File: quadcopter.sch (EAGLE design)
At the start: 65 parts, among them J1 AVR_SPI_PRG_6NS, Q1 N-CHANNEL_MOSFET, Q2 N-CHANNEL_MOSFET, Q3 N-CHANNEL_MOSFET, Q4 N-CHANNEL_MOSFET, U1 ATMEGA128RFA1

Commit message: Did board work, renamed flyback and filtered in schematic
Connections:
- removed net FILTERED: Q1.GND, Q2.GND, Q3.GND, Q4.GND, R10.2, R11.2, R2.2, R3.2, R4.2, R7.2, R8.2, R9.2
- removed net FLYBACK: D1.A, D6.A, D7.A, D8.A, Q1.D, Q2.D, Q3.D, Q4.D, U$1.V-, U$2.V-, U$3.V-, U$4.V-
- new net FILTERED1: Q1.GND, R2.2, R3.2
- new net FILTERED2: Q2.GND, R4.2, R7.2
- new net FILTERED3: Q3.GND, R8.2, R9.2
- new net FILTERED4: Q4.GND, R10.2, R11.2
- new net FLYBACK1: D1.A, Q1.D, U$1.V-
- new net FLYBACK2: D6.A, Q2.D, U$2.V-
- new net FLYBACK3: D7.A, Q3.D, U$3.V-
- new net FLYBACK4: D8.A, Q4.D, U$4.V-

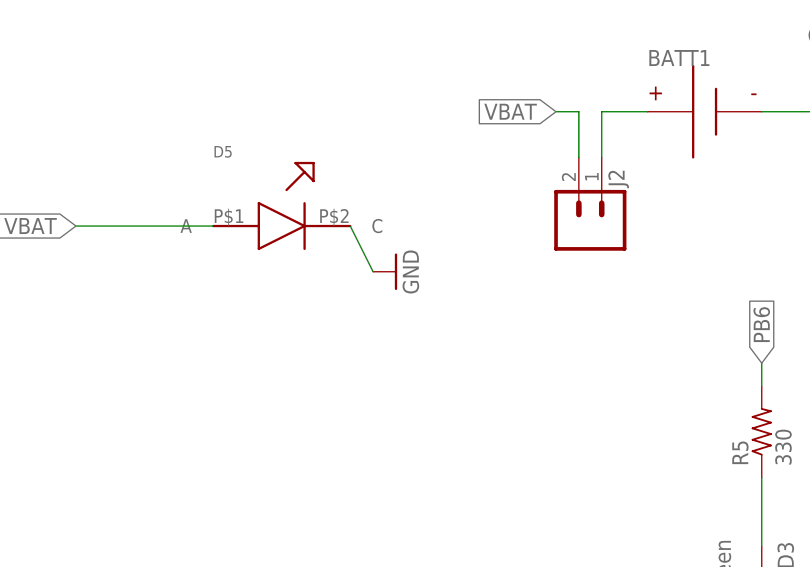
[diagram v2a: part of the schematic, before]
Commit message: Changed ground on LED to batgnd"
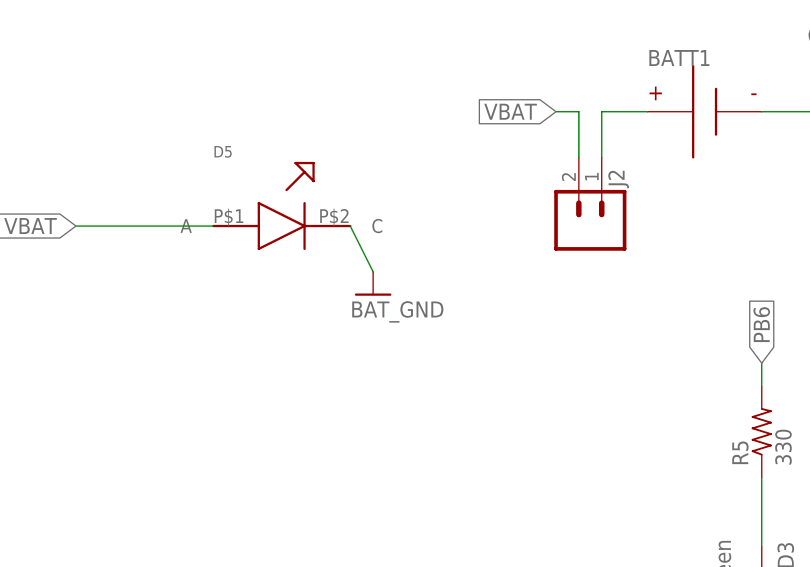
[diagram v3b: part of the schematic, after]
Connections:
- net BAT_GND: now also D5.C
- net GND: no longer D5.C
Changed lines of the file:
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@@
 <part name="P+12" library="quadparts_prebuilt" deviceset="VCC" device=""/>
 <part name="D5" library="LED" deviceset="BLUE_LED" device=""/>
-<part name="GND40" library="quadparts_prebuilt" deviceset="GND" device=""/>
 <part name="FRAME1" library="quadparts_prebuilt" deviceset="FRAME_B_L" device=""/>
 <part name="GND20" library="quadparts_prebuilt" deviceset="BAT_GND" device=""/>
@@
 <part name="C13" library="quadparts_prebuilt" deviceset="CAPACITOR-NP_" device="SMD-2012-0805_CERAMIC-0.1UF" value="0.1uF"/>
 <part name="C16" library="quadparts_prebuilt" deviceset="CAPACITOR-NP_" device="SMD-2012-0805_CERAMIC-0.1UF" value="0.1uF"/>
+<part name="GND40" library="quadparts_prebuilt" deviceset="BAT_GND" device=""/>
 </parts>
 <sheets>
@@
 <instance part="P+12" gate="VCC" x="-10.16" y="38.1" rot="R270"/>
 <instance part="D5" gate="G$1" x="-154.94" y="-12.7"/>
-<instance part="GND40" gate="1" x="-144.78" y="-17.78" rot="R90"/>
 <instance part="FRAME1" gate="G$1" x="-198.12" y="-220.98"/>
 <instance part="FRAME1" gate="G$2" x="127" y="-218.44"/>
@@
 <instance part="C13" gate="G$1" x="30.48" y="-180.34"/>
 <instance part="C16" gate="G$1" x="144.78" y="-149.86"/>
+<instance part="GND40" gate="1" x="-147.32" y="-20.32"/>
 </instances>
 <busses>
@@
 <pinref part="GND39" gate="1" pin="GND"/>
 <wire x1="-58.42" y1="7.62" x2="-55.88" y2="7.62" width="0.1524" layer="91"/>
-</segment>
-<segment>
-<pinref part="D5" gate="G$1" pin="C"/>
-<pinref part="GND40" gate="1" pin="GND"/>
-<wire x1="-149.86" y1="-12.7" x2="-147.32" y2="-17.78" width="0.1524" layer="91"/>
 </segment>
 <segment>
@@
 <pinref part="GND26" gate="1" pin="BAT_GND"/>
 </segment>
-</net>
+<segment>
+<pinref part="D5" gate="G$1" pin="C"/>
+<wire x1="-149.86" y1="-12.7" x2="-147.32" y2="-17.78" width="0.1524" layer="91"/>
+<pinref part="GND40" gate="1" pin="BAT_GND"/>
+</segment>
+</net>

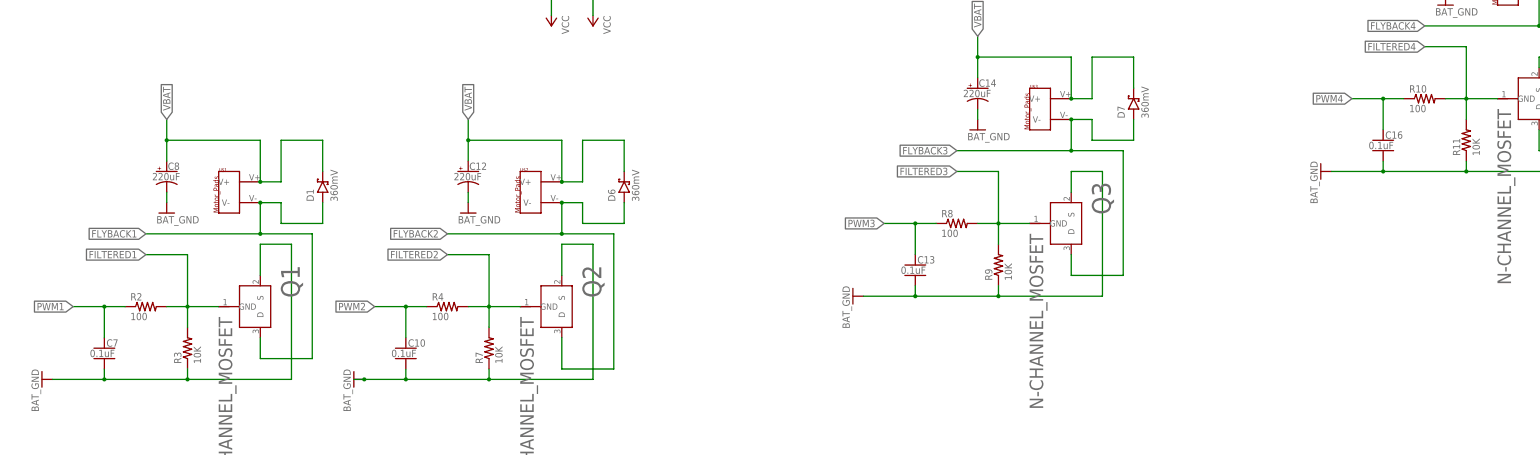
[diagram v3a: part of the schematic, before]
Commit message: Made most of swanson changes. Did not add reset button yet and did not autoroute and did not add in holes yet
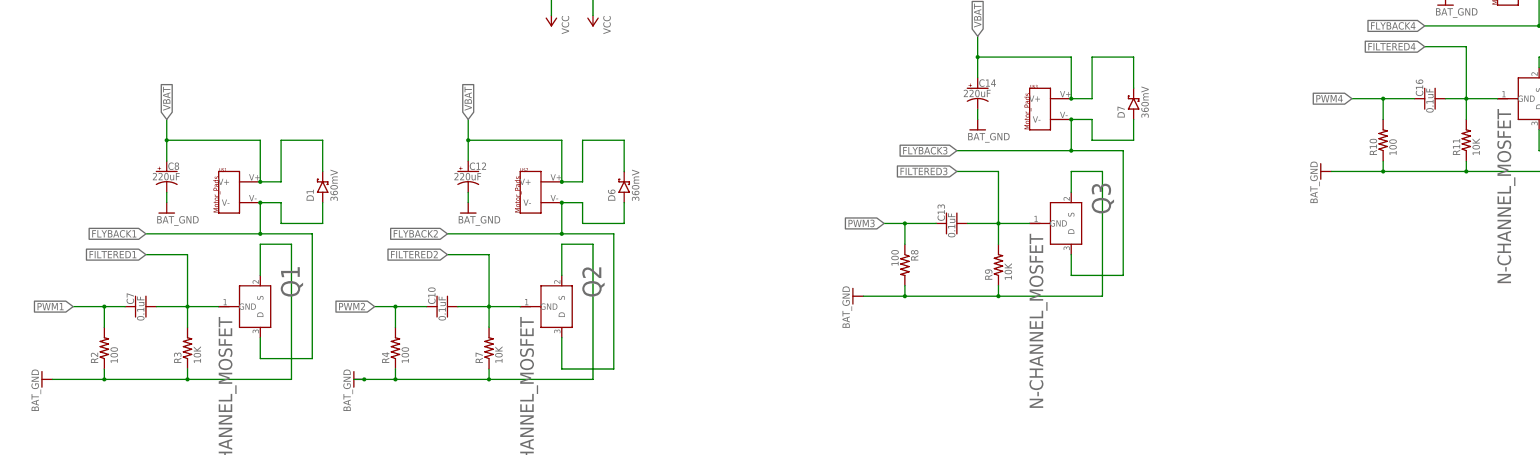
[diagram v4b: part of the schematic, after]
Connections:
- net BAT_GND: now also R10.1, R2.1, R4.1, R8.2; no longer C10.2, C13.2, C16.2, C7.2
- net FILTERED1: now also C7.2; no longer R2.2
- net FILTERED2: now also C10.2; no longer R4.2
- net FILTERED3: now also C13.2; no longer R8.2
- net FILTERED4: now also C16.2; no longer R10.2
- net PWM1: now also R2.2; no longer R2.1
- net PWM2: now also R4.2; no longer R4.1
- net PWM4: now also R10.2; no longer R10.1
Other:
- moved on the sheet: C10, C13, C16, C7, R10, R2, R4, R8

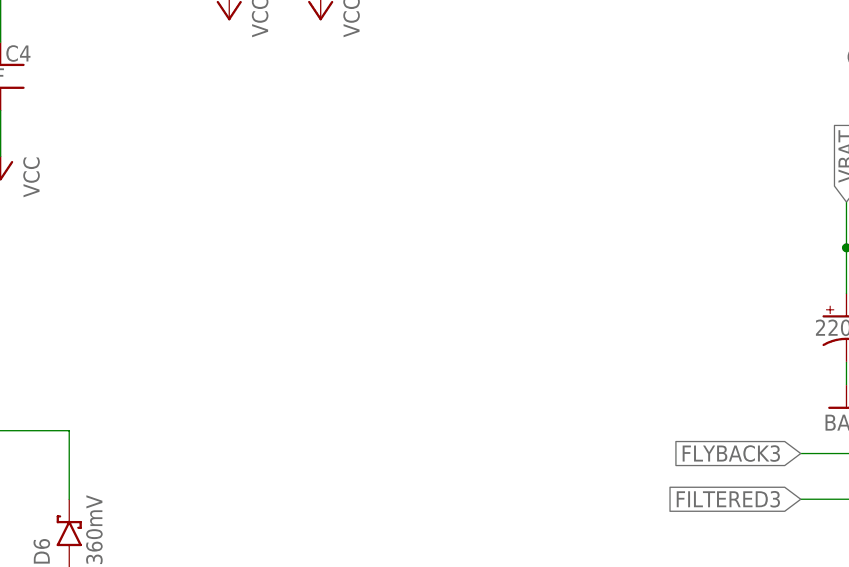
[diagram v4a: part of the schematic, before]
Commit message: added reset button and did autorouting
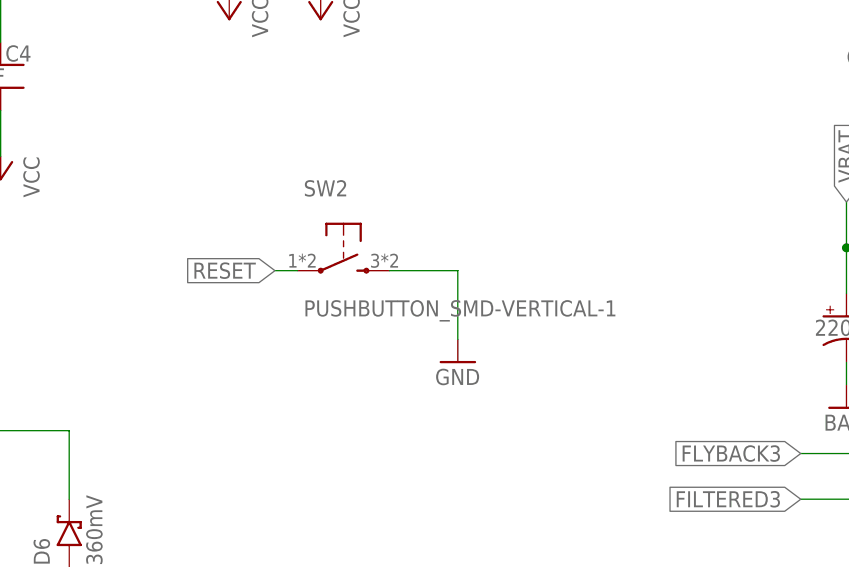
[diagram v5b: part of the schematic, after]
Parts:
- added SW2: PUSHBUTTON_SMD-VERTICAL-1, quadparts_prebuilt:PUSHBUTTON_SMD-VERTICAL-1
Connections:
- net GND: now also SW2.2
- net RESET: now also SW2.1
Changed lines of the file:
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@@
 <?xml version="1.0" encoding="utf-8"?>
 <!DOCTYPE eagle SYSTEM "eagle.dtd">
-<eagle version="8.1.1">
+<eagle version="8.2.0">
 <drawing>
 <settings>
@@
 <part name="C16" library="quadparts_prebuilt" deviceset="CAPACITOR-NP_" device="SMD-2012-0805_CERAMIC-0.1UF" value="0.1uF"/>
 <part name="GND40" library="quadparts_prebuilt" deviceset="BAT_GND" device=""/>
+<part name="SW2" library="quadparts_prebuilt" deviceset="PUSHBUTTON_" device="SMD-VERTICAL-1"/>
+<part name="GND42" library="quadparts_prebuilt" deviceset="GND" device=""/>
 </parts>
 <sheets>
@@
 <instance part="C16" gate="G$1" x="154.94" y="-139.7" rot="R90"/>
 <instance part="GND40" gate="1" x="-147.32" y="-20.32"/>
+<instance part="SW2" gate="G$1" x="-10.16" y="-129.54"/>
+<instance part="GND42" gate="1" x="2.54" y="-142.24"/>
 </instances>
 <busses>
@@
 <pinref part="GND41" gate="1" pin="GND"/>
 <wire x1="177.8" y1="-35.56" x2="172.72" y2="-35.56" width="0.1524" layer="91"/>
+</segment>
+<segment>
+<pinref part="GND42" gate="1" pin="GND"/>
+<wire x1="2.54" y1="-139.7" x2="2.54" y2="-132.08" width="0.1524" layer="91"/>
+<pinref part="SW2" gate="G$1" pin="2"/>
+<wire x1="2.54" y1="-132.08" x2="-5.08" y2="-132.08" width="0.1524" layer="91"/>
 </segment>
 </net>
@@
 <label x="43.18" y="25.4" size="1.778" layer="95" xref="yes"/>
 </segment>
-</net>
+<segment>
+<pinref part="SW2" gate="G$1" pin="1"/>
+<wire x1="-15.24" y1="-132.08" x2="-17.78" y2="-132.08" width="0.1524" layer="91"/>
+<label x="-17.78" y="-132.08" size="1.778" layer="95" rot="R180" xref="yes"/>
+</segment>
+</net>

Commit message: Made all changes specified in design review. Except LED
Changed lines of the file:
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@@
 <?xml version="1.0" encoding="utf-8"?>
 <!DOCTYPE eagle SYSTEM "eagle.dtd">
-<eagle version="8.2.0">
+<eagle version="8.1.1">
 <drawing>
 <settings>

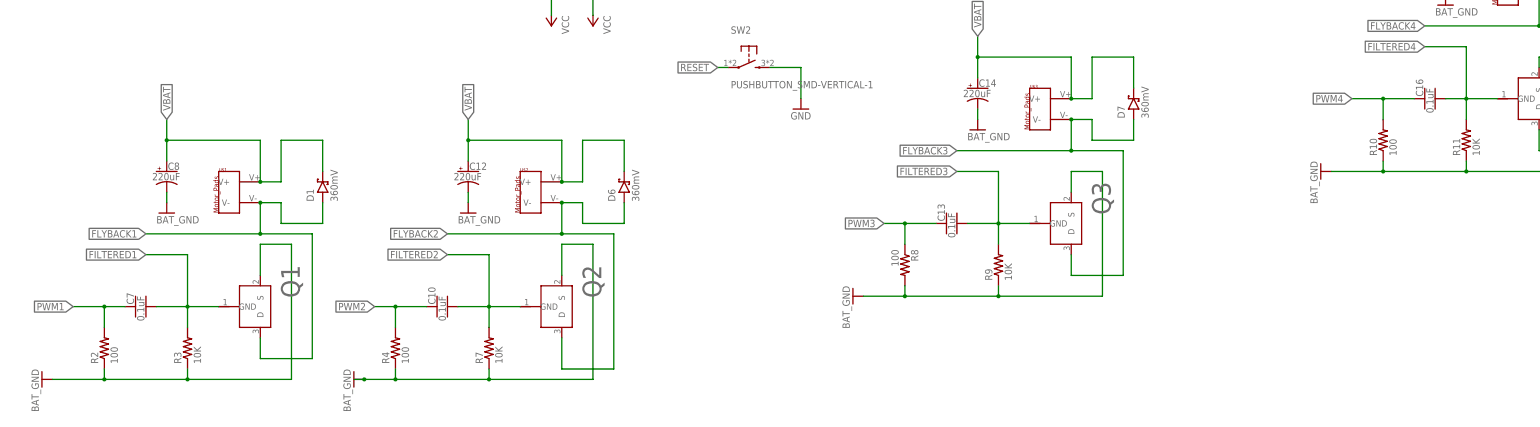
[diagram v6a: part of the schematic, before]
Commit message: Changed the resistor and capacitor placements in the motor drivers
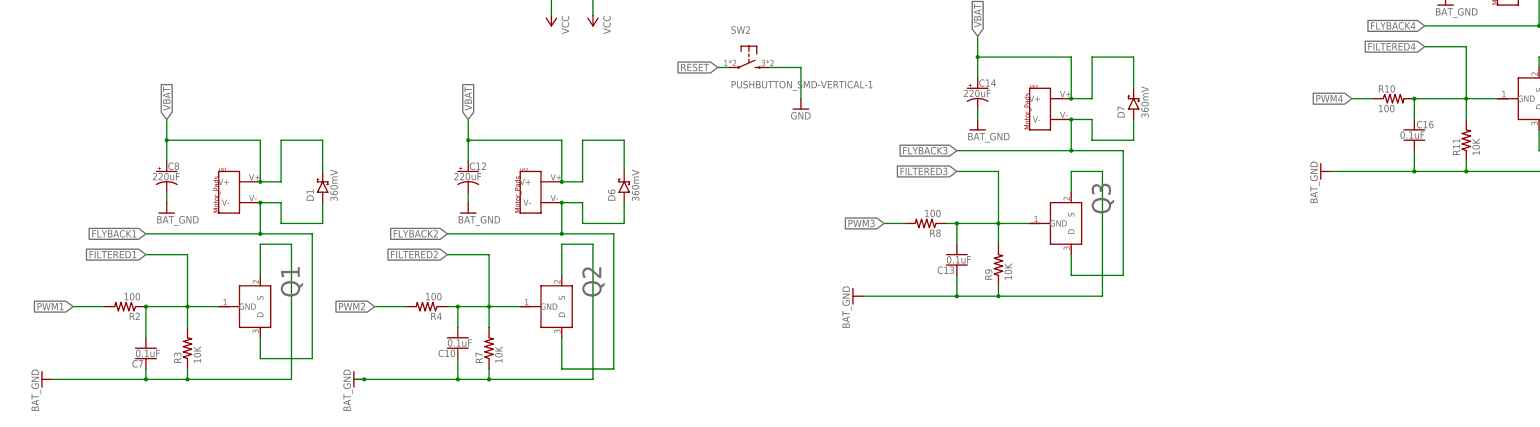
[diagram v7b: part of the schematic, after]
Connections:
- net BAT_GND: now also C10.1, C13.1, C16.2, C7.1; no longer R10.1, R2.1, R4.1, R8.2
- net FILTERED1: now also R2.1
- net FILTERED2: now also R4.1
- net FILTERED3: now also R8.1
- net FILTERED4: now also C16.1, R10.2; no longer C16.2
- net PWM1: no longer C7.1
- net PWM2: no longer C10.1
- net PWM3: now also R8.2; no longer C13.1, R8.1
- net PWM4: now also R10.1; no longer C16.1, R10.2
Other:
- moved on the sheet: C10, C13, C16, C7, R10, R2, R4, R8
